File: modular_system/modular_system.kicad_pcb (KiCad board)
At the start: 2 copper layers, 96.8 x 48.5 mm, 12 parts, among them J1 Screw_Terminal_01x02, J2 Conn_01x01_Male, J3 Conn_01x01_Male, J4 Conn_01x01_Male, J5 Conn_01x01_Male, J6 Conn_01x04_Female, J7 Conn_01x04_Female, U1 BluePill_STM32F103C

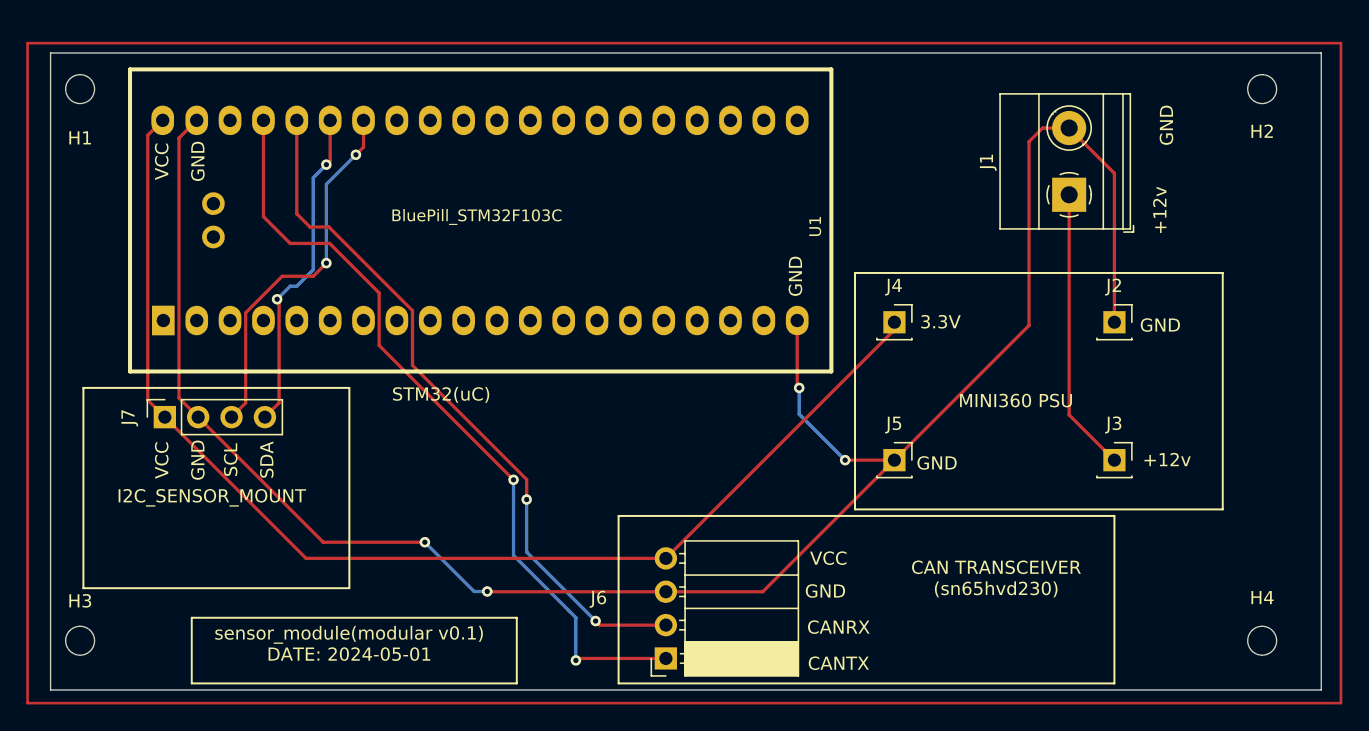
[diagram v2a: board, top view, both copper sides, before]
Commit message: shifted the I2C connector for better spacing
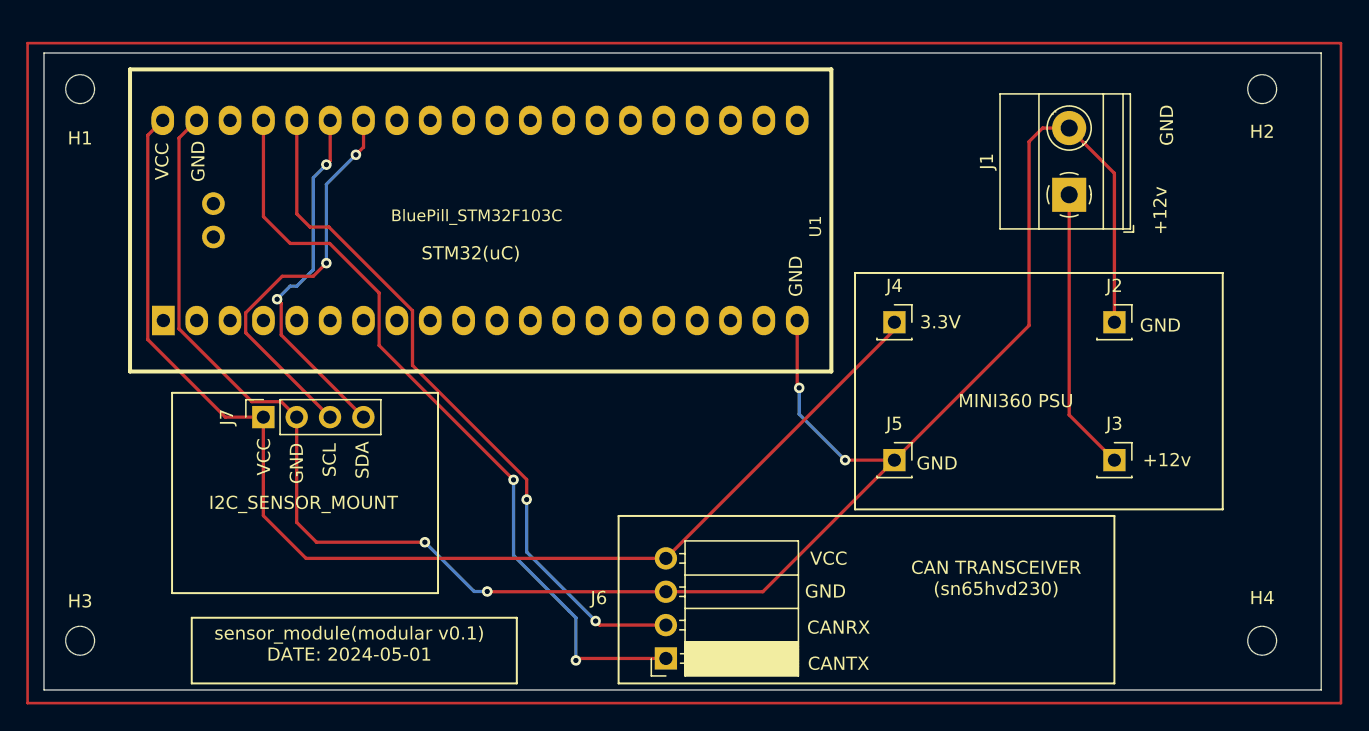
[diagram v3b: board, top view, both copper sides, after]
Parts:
- moved J7 7.50 mm to (117.7, 78.2)
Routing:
- net /SCL: track 28.1 -> 30.4 mm
- net /SDA: track 25.4 -> 27.5 mm
- net /Vcc: track 91.4 -> 93.1 mm
- net GND: track 150.5 -> 152.1 mm
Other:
- board size 96.8 x 48.5 mm -> 97.2 x 48.5 mm
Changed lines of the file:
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@@
   (net 41 "unconnected-(U1-Pad41)")
   (net 42 "unconnected-(U1-Pad42)")
-  (footprint "Connector_PinSocket_2.54mm:PinSocket_1x04_P2.54mm_Vertical" locked (layer "F.Cu")
-    (at 110.2 78.225 90)
+  (footprint "Connector_PinSocket_2.54mm:PinSocket_1x04_P2.54mm_Vertical" (layer "F.Cu")
+    (at 117.7 78.225 90)
     (descr "Through hole straight socket strip, 1x04, 2.54mm pitch, single row (from Kicad 4.0.7), script generated")
     (tags "Through hole socket strip THT 1x04 2.54mm single row")
@@
       (effects (font (size 1 1) (thickness 0.15)))
     )
-    (fp_text value "Conn_01x04_Female" (at -3.275 4.05 180) (layer "F.Fab")
+    (fp_text value "Conn_01x04_Female" (at -12.025 3.3 180) (layer "F.Fab")
       (effects (font (size 1 1) (thickness 0.15)))
     )
@@
   )
   (gr_rect (start 99.75 49.75) (end 199.75 100) (layer "F.Cu") (width 0.2) (fill none))
-  (gr_rect (start 104 76) (end 124.25 91.25) (layer "F.SilkS") (width 0.15) (fill none))
+  (gr_rect (start 110.75 76.375) (end 131 91.625) (layer "F.SilkS") (width 0.15) (fill none))
   (gr_rect (start 112.25 93.5) (end 137 98.5) (layer "F.SilkS") (width 0.15) (fill none))
   (gr_rect (start 144.75 85.75) (end 182.5 98.5) (layer "F.SilkS") (width 0.15) (fill none))
   (gr_rect (start 162.75 67.25) (end 190.75 85.25) (layer "F.SilkS") (width 0.15) (fill none))
-  (gr_rect (start 101.5 50.5) (end 198.25 99) (layer "Edge.Cuts") (width 0.1) (fill none))
+  (gr_rect (start 101 50.5) (end 198.25 99) (layer "Edge.Cuts") (width 0.1) (fill none))
   (gr_text "CANTX" (at 161.5 97) (layer "F.SilkS")
     (effects (font (size 1 1) (thickness 0.15)))
@@
     (effects (font (size 1 1) (thickness 0.15)))
   )
-  (gr_text "SCL" (at 115.25 81.5 90) (layer "F.SilkS")
-    (effects (font (size 1 1) (thickness 0.15)))
-  )
-  (gr_text "SDA" (at 118 81.5 90) (layer "F.SilkS")
+  (gr_text "SCL" (at 122.75 81.5 90) (layer "F.SilkS")
+    (effects (font (size 1 1) (thickness 0.15)))
+  )
+  (gr_text "SDA" (at 125.25 81.5 90) (layer "F.SilkS")
     (effects (font (size 1 1) (thickness 0.15)))
   )
@@
     (effects (font (size 1 1) (thickness 0.15)))
   )
-  (gr_text "GND" (at 112.75 81.5 90) (layer "F.SilkS")
+  (gr_text "GND" (at 120.25 81.75 90) (layer "F.SilkS")
     (effects (font (size 1 1) (thickness 0.15)))
   )
@@
     (effects (font (size 1 1) (thickness 0.15)))
   )
-  (gr_text "STM32(uC)" (at 131.25 76.5) (layer "F.SilkS")
+  (gr_text "STM32(uC)" (at 133.5 65.75) (layer "F.SilkS")
     (effects (font (size 1 1) (thickness 0.15)))
   )
@@
     (effects (font (size 1 1) (thickness 0.15)))
   )
-  (gr_text "VCC" (at 110 81.5 90) (layer "F.SilkS")
+  (gr_text "VCC" (at 117.75 81.25 90) (layer "F.SilkS")
     (effects (font (size 1 1) (thickness 0.15)))
   )
@@
     (effects (font (size 1 1) (thickness 0.15)))
   )
-  (gr_text "I2C_SENSOR_MOUNT" (at 113.75 84.25) (layer "F.SilkS")
+  (gr_text "I2C_SENSOR_MOUNT" (at 120.75 84.75) (layer "F.SilkS")
     (effects (font (size 1 1) (thickness 0.15)))
   )
@@
   (segment (start 179.055 78.055) (end 179.055 61.295) (width 0.25) (layer "F.Cu") (net 1))
   (segment (start 182.5 81.5) (end 179.055 78.055) (width 0.25) (layer "F.Cu") (net 1))
-  (segment (start 120.955 88.98) (end 110.2 78.225) (width 0.25) (layer "F.Cu") (net 2))
+  (segment (start 117.7 78.225) (end 114.806578 78.225) (width 0.25) (layer "F.Cu") (net 2))
+  (segment (start 108.901089 72.319511) (end 108.901089 56.767311) (width 0.25) (layer "F.Cu") (net 2))
   (segment (start 165.75 71.58) (end 148.35 88.98) (width 0.25) (layer "F.Cu") (net 2))
   (segment (start 165.75 71) (end 165.75 71.58) (width 0.25) (layer "F.Cu") (net 2))
-  (segment (start 110.2 78.225) (end 108.901089 76.926089) (width 0.25) (layer "F.Cu") (net 2))
-  (segment (start 108.901089 76.926089) (end 108.901089 56.767311) (width 0.25) (layer "F.Cu") (net 2))
+  (segment (start 117.7 78.225) (end 117.7 85.725) (width 0.25) (layer "F.Cu") (net 2))
   (segment (start 108.901089 56.767311) (end 110.0384 55.63) (width 0.25) (layer "F.Cu") (net 2))
   (segment (start 148.35 88.98) (end 120.955 88.98) (width 0.25) (layer "F.Cu") (net 2))
-  (segment (start 111.277311 56.981889) (end 111.277311 76.762311) (width 0.25) (layer "F.Cu") (net 3))
+  (segment (start 114.806578 78.225) (end 108.901089 72.319511) (width 0.25) (layer "F.Cu") (net 2))
+  (segment (start 117.7 85.725) (end 120.955 88.98) (width 0.25) (layer "F.Cu") (net 2))
+  (segment (start 116.8278 77.050489) (end 111.277311 71.5) (width 0.25) (layer "F.Cu") (net 3))
   (segment (start 134.77 91.52) (end 134.75 91.5) (width 0.25) (layer "F.Cu") (net 3))
   (segment (start 158.3492 75.8492) (end 158.5 76) (width 0.25) (layer "F.Cu") (net 3))
-  (segment (start 122.265 87.75) (end 130 87.75) (width 0.25) (layer "F.Cu") (net 3))
-  (segment (start 112.74 78.225) (end 122.265 87.75) (width 0.25) (layer "F.Cu") (net 3))
+  (segment (start 119.065489 77.050489) (end 116.8278 77.050489) (width 0.25) (layer "F.Cu") (net 3))
   (segment (start 148.35 91.52) (end 134.77 91.52) (width 0.25) (layer "F.Cu") (net 3))
+  (segment (start 120.24 78.225) (end 119.065489 77.050489) (width 0.25) (layer "F.Cu") (net 3))
   (segment (start 182.5 71) (end 182.5 59.66) (width 0.25) (layer "F.Cu") (net 3))
   (segment (start 155.73 91.52) (end 165.75 81.5) (width 0.25) (layer "F.Cu") (net 3))
@@
   (segment (start 158.3492 70.87) (end 158.3492 75.8492) (width 0.25) (layer "F.Cu") (net 3))
   (segment (start 176 71.25) (end 176 57.25) (width 0.25) (layer "F.Cu") (net 3))
+  (segment (start 130 87.75) (end 121.75 87.75) (width 0.25) (layer "F.Cu") (net 3))
+  (segment (start 120.24 86.24) (end 120.24 78.225) (width 0.25) (layer "F.Cu") (net 3))
   (segment (start 182.5 59.66) (end 179.055 56.215) (width 0.25) (layer "F.Cu") (net 3))
   (segment (start 165.75 81.5) (end 176 71.25) (width 0.25) (layer "F.Cu") (net 3))
   (segment (start 148.35 91.52) (end 155.73 91.52) (width 0.25) (layer "F.Cu") (net 3))
+  (segment (start 111.277311 71.5) (end 111.277311 56.981889) (width 0.25) (layer "F.Cu") (net 3))
+  (segment (start 177.035 56.215) (end 179.055 56.215) (width 0.25) (layer "F.Cu") (net 3))
   (segment (start 112.6292 55.63) (end 111.277311 56.981889) (width 0.25) (layer "F.Cu") (net 3))
-  (segment (start 111.277311 76.762311) (end 112.74 78.225) (width 0.25) (layer "F.Cu") (net 3))
-  (segment (start 177.035 56.215) (end 179.055 56.215) (width 0.25) (layer "F.Cu") (net 3))
+  (segment (start 121.75 87.75) (end 120.24 86.24) (width 0.25) (layer "F.Cu") (net 3))
   (segment (start 165.75 81.5) (end 162 81.5) (width 0.25) (layer "F.Cu") (net 3))
   (via (at 134.75 91.5) (size 0.8) (drill 0.4) (layers "F.Cu" "B.Cu") (net 3))
@@
   (segment (start 137.75 88.5) (end 137.75 84.5) (width 0.25) (layer "B.Cu") (net 5))
   (segment (start 121.5 67.5) (end 119.137545 67.5) (width 0.25) (layer "F.Cu") (net 38))
-  (segment (start 116.35732 77.14768) (end 115.28 78.225) (width 0.25) (layer "F.Cu") (net 38))
   (segment (start 119.137545 67.5) (end 116.35732 70.280225) (width 0.25) (layer "F.Cu") (net 38))
+  (segment (start 116.35732 71.80232) (end 116.35732 70.280225) (width 0.25) (layer "F.Cu") (net 38))
+  (segment (start 122.78 78.225) (end 116.35732 71.80232) (width 0.25) (layer "F.Cu") (net 38))
   (segment (start 124.75 58.25) (end 125.3292 57.6708) (width 0.25) (layer "F.Cu") (net 38))
   (segment (start 125.3292 57.6708) (end 125.3292 55.63) (width 0.25) (layer "F.Cu") (net 38))
   (segment (start 122.5 66.5) (end 121.5 67.5) (width 0.25) (layer "F.Cu") (net 38))
-  (segment (start 116.35732 70.280225) (end 116.35732 77.14768) (width 0.25) (layer "F.Cu") (net 38))
   (via (at 122.5 66.5) (size 0.8) (drill 0.4) (layers "F.Cu" "B.Cu") (net 38))
   (via (at 124.75 58.25) (size 0.8) (drill 0.4) (layers "F.Cu" "B.Cu") (net 38))
   (segment (start 122.5 60.5) (end 124.75 58.25) (width 0.25) (layer "B.Cu") (net 38))
   (segment (start 122.5 66.5) (end 122.5 60.5) (width 0.25) (layer "B.Cu") (net 38))
-  (segment (start 118.89732 77.14768) (end 118.89732 69.10268) (width 0.25) (layer "F.Cu") (net 39))
-  (segment (start 117.82 78.225) (end 118.89732 77.14768) (width 0.25) (layer "F.Cu") (net 39))
+  (segment (start 119.06108 71.96608) (end 119.06108 69.56108) (width 0.25) (layer "F.Cu") (net 39))
   (segment (start 122.7892 55.63) (end 122.7892 58.7108) (width 0.25) (layer "F.Cu") (net 39))
+  (segment (start 125.32 78.225) (end 119.06108 71.96608) (width 0.25) (layer "F.Cu") (net 39))
   (segment (start 122.7892 58.7108) (end 122.5 59) (width 0.25) (layer "F.Cu") (net 39))
+  (segment (start 119.06108 69.56108) (end 118.75 69.25) (width 0.25) (layer "F.Cu") (net 39))
   (segment (start 118.89732 69.10268) (end 118.75 69.25) (width 0.25) (layer "F.Cu") (net 39))
   (via (at 122.5 59) (size 0.8) (drill 0.4) (layers "F.Cu" "B.Cu") (net 39))
